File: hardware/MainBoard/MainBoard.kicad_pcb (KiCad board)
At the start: 2 copper layers, 56.9 x 28.9 mm, 25 parts, among them J1 Therm., J2 SSR, J3 Serial, J4 5Vin, J6 Keypad1, SW1 Boot Mode, SW2 RESET, U1 ESP-12F, U2 AMS1117-3.3

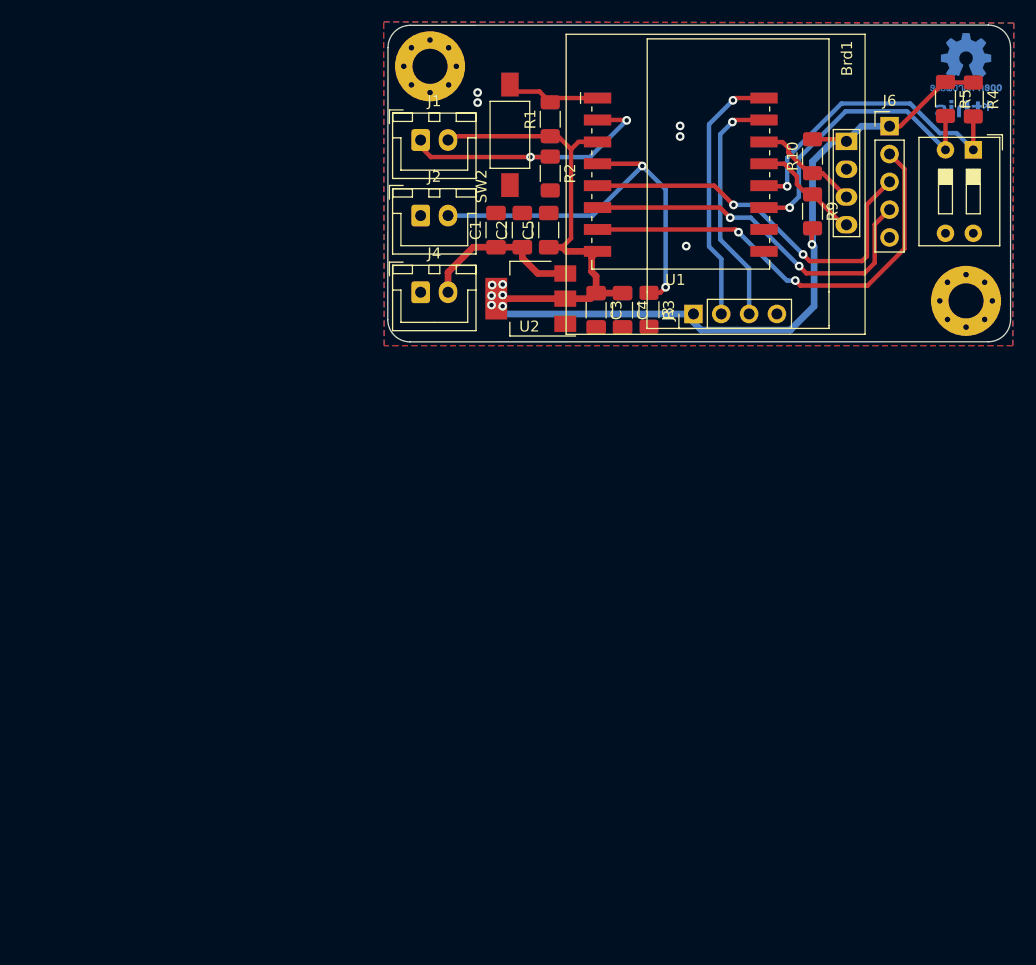
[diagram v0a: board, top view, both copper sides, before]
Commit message: gme12864 replaced with ssd1306
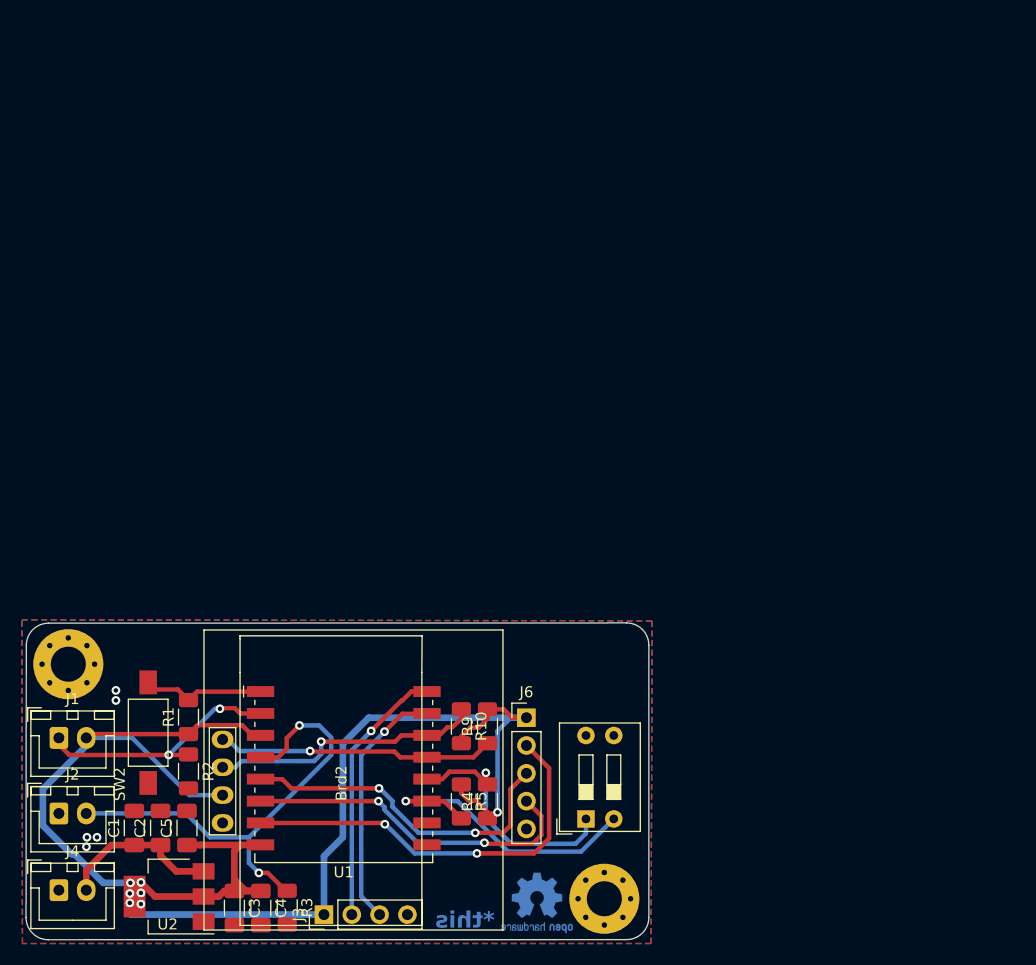
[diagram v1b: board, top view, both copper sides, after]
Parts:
- removed Brd1: GME12864_OLED, SSD1306:GME12864_OLED
- added Brd2: SSD1306, SSD1306:128x64OLED, F.Cu at (40.5, 183.7)
- U1: footprint RF_Module:ESP-07 -> ESP8266:ESP-07-RF_Modules
- moved REF** 86.1 mm to (58.6, 194.7)
- moved R4 78.0 mm to (54.1, 185.4), turned to 90 degrees
- moved R5 77.9 mm to (51.7, 185.4)
- moved SW1 70.6 mm to (63.1, 187.0), turned to 90 degrees
- moved J3 64.4 mm to (39.2, 195.7)
- moved C2 63.8 mm to (24.2, 187.8)
- moved C3 63.8 mm to (31.0, 195.1)
- moved C4 63.8 mm to (33.4, 195.1)
- moved J1 63.8 mm to (15.0, 179.6)
- moved J2 63.8 mm to (15.0, 186.5)
- moved J4 63.8 mm to (15.0, 193.5)
- moved R1 63.8 mm to (26.8, 177.7)
- moved REF** 63.8 mm to (15.8, 172.9)
- moved U2 63.8 mm to (25.0, 194.1)
- moved C1 63.8 mm to (21.8, 187.8)
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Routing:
- net +3V3: track 120.3 -> 164.2 mm
- net /SCK: track 9.86 -> 25.1 mm, vias 0 -> 1
- net /SDA: track 10.3 -> 25.4 mm, vias 0 -> 1
- net /IO16: track 37.5 -> 43.6 mm
- net /IO00: track 28.6 -> 23.4 mm
- net /IO14: track 35.3 -> 30.8 mm
- net /IO13: track 40.8 -> 37.4 mm
- net /A0: track 25.7 -> 23.2 mm
- net /RESET: track 8.57 -> 11.0 mm
- net /IO12: track 33.6 -> 31.4 mm
- net /IO02: track 26.9 -> 27.9 mm
- net /RX: track 22.0 -> 22.8 mm

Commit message: libraries updated
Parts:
- removed Brd2: SSD1306, SSD1306:128x64OLED
- added Brd1: SSD1306, SSD1306:128x64OLED, F.Cu at (40.5, 183.7)
